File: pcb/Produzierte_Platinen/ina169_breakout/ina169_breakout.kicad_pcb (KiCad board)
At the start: 2 copper layers, 23 x 21.7 mm, 6 parts, among them J1 INA169 Breakout 2.5A / 5A (sh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, U1 INA169_IC

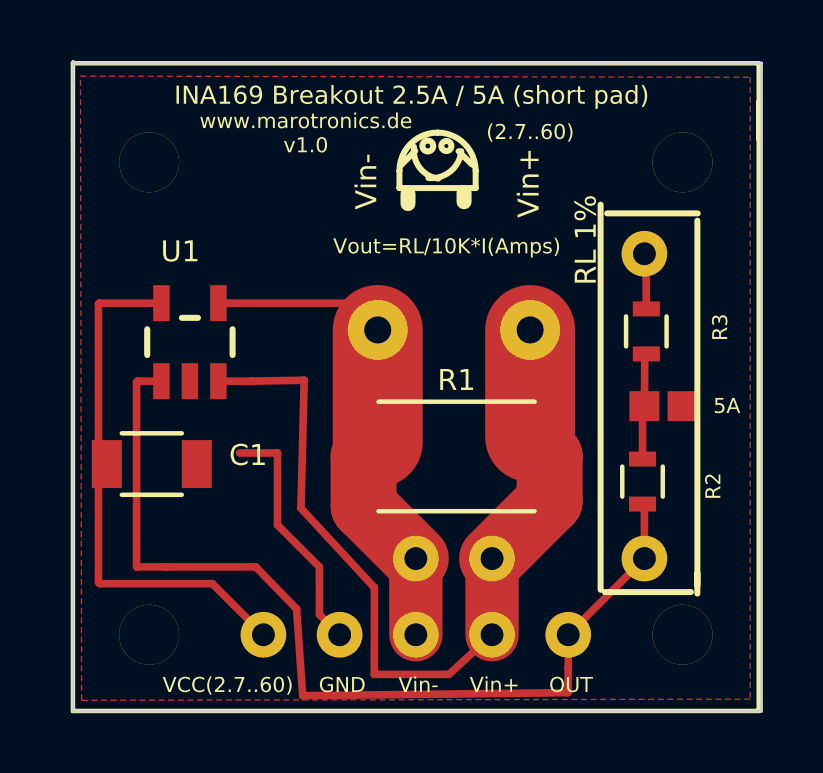
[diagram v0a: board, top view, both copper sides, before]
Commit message: ina169_breakout
3D Ansichten aktualisiert
Namen von Footprints umgeändert und angepasst an die neuen Bezeichnungen
von Kicad
----- keine Änderungen am Schaltplan vorgenommen -----
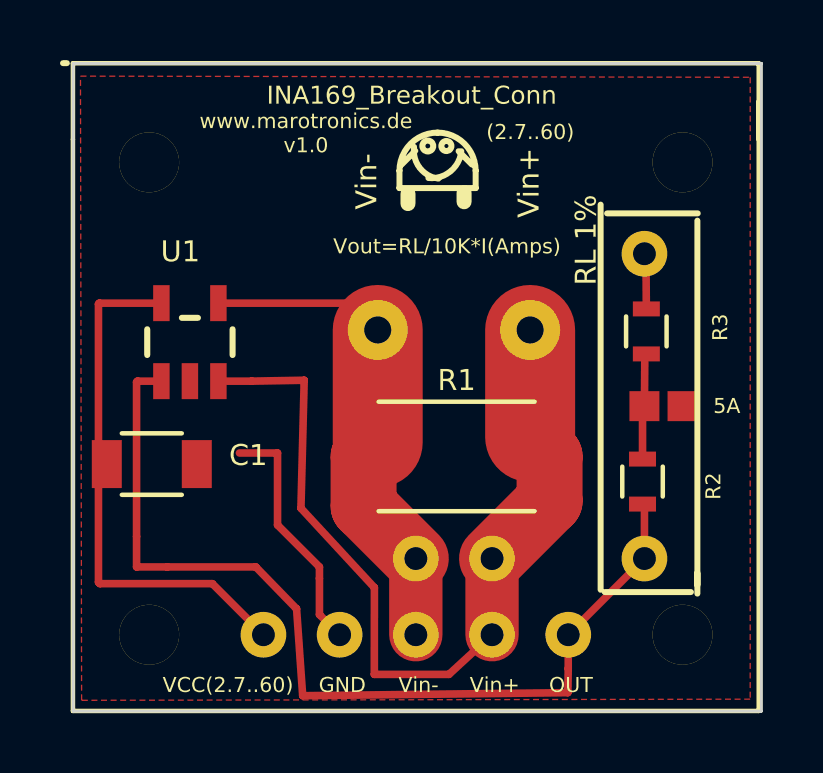
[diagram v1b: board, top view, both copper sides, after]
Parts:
- J1: value INA169 Breakout 2.5A / 5A (short pad) -> INA169_Breakout_Conn
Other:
- board size 23 x 21.7 mm -> 22.9 x 21.6 mm
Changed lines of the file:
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@@
-(kicad_pcb (version 4) (host pcbnew "(2015-01-13 BZR 5369)-product")
+(kicad_pcb (version 20160815) (host pcbnew "(2017-01-09 revision c2fb336)-makepkg")
   (general
     (links 19)
     (no_connects 0)
-    (area 136.995699 93.465179 160.070001 115.218681)
+    (area 137.029999 93.529999 160.070001 115.220001)
     (thickness 1.6)
-    (drawings 37)
+    (drawings 38)
     (tracks 57)
     (zones 0)
@@
       (hpglpenspeed 20)
       (hpglpendiameter 15)
-      (hpglpenoverlay 2)
       (psnegative false)
       (psa4output false)
@@
       (effects (font (size 1.5 1.5) (thickness 0.15)))
     )
-    (fp_text value "INA169 Breakout 2.5A / 5A (short pad)" (at -0.137145 -10.35925) (layer F.SilkS)
+    (fp_text value INA169_Breakout_Conn (at -0.137145 -10.35925) (layer F.SilkS)
       (effects (font (size 0.6 0.6) (thickness 0.1)))
     )
@@
     (pad 2 smd rect (at 3.1 0 180) (size 1 3.2) (layers F.Cu F.Paste F.Mask)
       (net 3 "Net-(J1-Pad3)"))
-    (model Resistors_SMD/R_2512.wrl
-      (at (xyz 0 0 0))
-      (scale (xyz 1 1 1))
-      (rotate (xyz 0 0 0))
+    (model ${KISYS3DMOD}/Resistors_SMD.3dshapes/R_2512.wrl
+      (at (xyz 0 0 0))
+      (scale (xyz 1 1 1))
+      (rotate (xyz 0 0 180))
     )
   )
@@
     (pad 5 smd rect (at -0.95 -1.3001) (size 0.55 1.2) (layers F.Cu F.Paste F.Mask)
       (net 1 "Net-(C1-Pad1)"))
+    (model ${KISYS3DMOD}/TO_SOT_Packages_SMD.3dshapes/SOT-23-5.wrl
+      (at (xyz 0 0 0))
+      (scale (xyz 1 1 1))
+      (rotate (xyz 0 0 -90))
+    )
   )
   (module Capacitors_SMD:C_1206 (layer F.Cu)
@@
     (pad 2 smd rect (at 1.5 0) (size 1 1.6) (layers F.Cu F.Paste F.Mask)
       (net 2 GND))
-    (model Capacitors_SMD/C_1206.wrl
+    (model ${KISYS3DMOD}/Capacitors_SMD.3dshapes/C_1206.wrl
       (at (xyz 0 0 0))
       (scale (xyz 1 1 1))
@@
     (pad 2 smd rect (at 0.75 0 90) (size 0.5 0.9) (layers F.Cu F.Paste F.Mask)
       (net 6 "Net-(R2-Pad2)"))
-    (model Resistors_SMD/R_0603.wrl
+    (model ${KISYS3DMOD}/Resistors_SMD.3dshapes/R_0603.wrl
       (at (xyz 0 0 0))
       (scale (xyz 1 1 1))
@@
     (pad 2 smd rect (at 0.75 0 90) (size 0.5 0.9) (layers F.Cu F.Paste F.Mask)
       (net 2 GND))
-    (model Resistors_SMD.3dshapes/R_0603.wrl
+    (model ${KISYS3DMOD}/Resistors_SMD.3dshapes/R_0603.wrl
       (at (xyz 0 0 0))
       (scale (xyz 1 1 1))
       (rotate (xyz 0 0 0))
     )
-    (model Resistors_SMD/R_0603.wrl
-      (at (xyz 0 0 0))
-      (scale (xyz 1 1 1))
-      (rotate (xyz 0 0 0))
-    )
-  )
+  )
+  (gr_line (start 160.02 115.17) (end 137.08 115.17) (angle 90) (layer Edge.Cuts) (width 0.1))
+  (gr_line (start 160.02 93.58) (end 160.02 115.17) (angle 90) (layer Edge.Cuts) (width 0.1))
+  (gr_line (start 137.08 93.58) (end 160.02 93.58) (angle 90) (layer Edge.Cuts) (width 0.1))
+  (gr_line (start 136.87 93.57) (end 136.74 93.57) (angle 90) (layer F.SilkS) (width 0.2))
+  (gr_line (start 137.08 115.16) (end 137.08 93.58) (angle 90) (layer Edge.Cuts) (width 0.1))
+  (gr_line (start 137.08 115.17) (end 137.08 115.16) (angle 90) (layer Edge.Cuts) (width 0.1))
   (gr_text 5A (at 158.86684 104.99852) (layer F.SilkS)
     (effects (font (size 0.5 0.5) (thickness 0.1)))
@@
     (effects (font (size 0.7 0.7) (thickness 0.1)))
   )
-  (gr_line (start 137.07364 93.51518) (end 137.07364 115.16868) (angle 90) (layer Edge.Cuts) (width 0.1))
-  (gr_line (start 160.02 93.57106) (end 160.02 115.16868) (angle 90) (layer Edge.Cuts) (width 0.1))
-  (gr_line (start 137.16 93.54312) (end 137.0457 93.54312) (angle 90) (layer Edge.Cuts) (width 0.1))
-  (gr_line (start 160.02 115.16868) (end 137.16 115.16868) (angle 90) (layer Edge.Cuts) (width 0.1))
-  (gr_line (start 137.07364 93.57106) (end 160.02 93.57106) (angle 90) (layer Edge.Cuts) (width 0.1))
-  (dimension 22.931388 (width 0.3) (layer B.Fab)
-    (gr_text "22,931 mm" (at 148.484532 119.46) (layer B.Fab)
+  (dimension 22.931388 (width 0.3) (layer Dwgs.User)
+    (gr_text "22,931 mm" (at 148.484532 119.46) (layer Dwgs.User)
       (effects (font (size 1.5 1.5) (thickness 0.3)))
     )
@@
     (arrow2b (pts (xy 137.018838 118.11) (xy 138.145342 117.523579)))
   )
-  (dimension 21.564616 (width 0.3) (layer B.Fab)
-    (gr_text "21,565 mm" (at 162.56 104.14 270) (layer B.Fab)
+  (dimension 21.564616 (width 0.3) (layer Dwgs.User)
+    (gr_text "21,565 mm" (at 162.56 104.14 270) (layer Dwgs.User)
       (effects (font (size 1.5 1.5) (thickness 0.3)))
     )
